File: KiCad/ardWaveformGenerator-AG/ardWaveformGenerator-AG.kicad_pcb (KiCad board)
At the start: 2 copper layers, 97.8 x 55.9 mm, 40 parts, among them SW1 SW_Rotary1x4, U1 Power in, U2 LM386, U3 Output

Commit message: ardWaveformGenerator-AG-pio with pcb-0.2
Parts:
- added R27: 10k, My_Misc:R_Axial_DIN0207_L6.3mm_D2.5mm_P10.16mm_Horizontal_large, F.Cu at (154.9, 107.6)
- added R28: 10k, My_Misc:R_Axial_DIN0207_L6.3mm_D2.5mm_P10.16mm_Horizontal_large, F.Cu at (154.9, 84.8)
- added R29: 10k, My_Misc:R_Axial_DIN0207_L6.3mm_D2.5mm_P10.16mm_Horizontal_large, F.Cu at (154.9, 72.1)
- added R30: 10k, My_Misc:R_Axial_DIN0207_L6.3mm_D2.5mm_P10.16mm_Horizontal_large, F.Cu at (150.5, 101.1)
- added R31: 10k, My_Misc:R_Axial_DIN0207_L6.3mm_D2.5mm_P10.16mm_Horizontal_large, F.Cu at (140.3, 97.9)
- added R32: 2.2k, My_Misc:R_Axial_DIN0207_L6.3mm_D2.5mm_P10.16mm_Horizontal_large, F.Cu at (150.5, 94.8)
- added R33: 220R, My_Misc:R_Axial_DIN0207_L6.3mm_D2.5mm_P10.16mm_Horizontal_large, F.Cu at (149.2, 81.0)
- added R34: 220R, My_Misc:R_Axial_DIN0207_L6.3mm_D2.5mm_P10.16mm_Horizontal_large, F.Cu at (146.1, 81.0)
- added R35: 220R, My_Misc:R_Axial_DIN0207_L6.3mm_D2.5mm_P10.16mm_Horizontal_large, F.Cu at (142.9, 81.0)
- added R36: 220R, My_Misc:R_Axial_DIN0207_L6.3mm_D2.5mm_P10.16mm_Horizontal_large, F.Cu at (139.7, 81.0)
- R1, R12, R14, R16, R18, R2, R20, R21, R4, R6: value 20k -> 10k; footprint My_Parts:R_Axial_parallell_DIN0207_L6.3mm_D2.5mm_P10.16mm_Horizontal_large -> My_Misc:R_Axial_DIN0207_L6.3mm_D2.5mm_P10.16mm_Horizontal_large
- R22: value 2.2k -> 10k
- R23, R24, R25, R26: value 220R -> 10k
- moved R26 113.0 mm to (158.1, 72.1)
- moved RV2 110.4 mm to (180.3, 125.4), turned to 180 degrees
- moved R25 103.8 mm to (158.1, 84.8)
- moved R11 102.9 mm to (186.7, 96.8), turned to 90 degrees
- moved R24 97.7 mm to (158.1, 107.6), turned to 90 degrees
- moved R23 95.0 mm to (161.3, 72.1)
- moved R10 91.6 mm to (170.8, 72.1), turned to -90 degrees
- moved R9 89.2 mm to (170.8, 84.8), turned to -90 degrees
- moved R8 87.0 mm to (170.8, 107.6), turned to 90 degrees
- moved R19 83.6 mm to (164.5, 84.8), turned to -90 degrees
- moved RV1 83.5 mm to (163.9, 124.4)
- moved R20 83.2 mm to (164.5, 72.1), turned to -90 degrees
- moved R2 82.8 mm to (183.5, 86.7), turned to -90 degrees
- moved D2 81.5 mm to (142.2, 77.2)
- moved D4 81.5 mm to (128.3, 77.2)
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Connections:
- A1 pad 27: D0 -> D12
- A1 pad 31: A4 -> unconnected-(A1-Pad31)
- A1 pad 32: A5 -> unconnected-(A1-Pad32)
- R1 pad 1: GND -> Net-(R1-Pad1)
- R1 pad 2: Net-(R1-Pad2) -> Net-(R5-Pad1)
- R10 pad 1: A2 -> D2
- R10 pad 2: +5V -> Net-(R10-Pad2)
- R11 pad 1: A3 -> A0
- R12 pad 1: D3 -> A1
- R12 pad 2: Net-(R12-Pad2) -> +5V
- R13 pad 1: Net-(R12-Pad2) -> A2
- R13 pad 2: Net-(R13-Pad2) -> +5V
- R14 pad 1: D4 -> A3
- R14 pad 2: Net-(R13-Pad2) -> +5V
- R15 pad 1: Net-(R13-Pad2) -> Net-(R8-Pad2)
- R15 pad 2: Net-(R15-Pad2) -> Net-(R18-Pad1)
- R16 pad 1: D5 -> Net-(R16-Pad1)
- R16 pad 2: Net-(R15-Pad2) -> Net-(R18-Pad1)
- R17 pad 1: Net-(R15-Pad2) -> D3
- R17 pad 2: Net-(R17-Pad2) -> Net-(R16-Pad1)
- R18 pad 1: D6 -> Net-(R18-Pad1)
- R18 pad 2: Net-(R17-Pad2) -> Net-(R18-Pad2)
- R19 pad 1: Net-(R17-Pad2) -> Net-(R19-Pad1)
- R19 pad 2: Net-(C1-Pad1) -> Net-(R18-Pad2)
- R2 pad 1: D0 -> GND
- R2 pad 2: Net-(R1-Pad2) -> Net-(R1-Pad1)
- R20 pad 1: D7 -> D4
- R20 pad 2: Net-(C1-Pad1) -> Net-(R19-Pad1)
- R21 pad 1: Net-(C1-Pad2) -> Net-(R18-Pad2)
- R22 pad 1: Net-(R21-Pad2) -> Net-(R22-Pad1)
- R22 pad 2: GND -> Net-(R21-Pad2)
- R23 pad 1: Net-(D1-Pad1) -> D5
- R23 pad 2: GND -> Net-(R22-Pad1)
- R24 pad 1: Net-(D2-Pad1) -> Net-(R21-Pad2)
- R24 pad 2: GND -> Net-(R24-Pad2)
- R25 pad 1: Net-(D3-Pad1) -> Net-(R25-Pad1)
- R25 pad 2: GND -> Net-(R24-Pad2)
- R26 pad 1: Net-(D4-Pad1) -> D6
- R26 pad 2: GND -> Net-(R25-Pad1)
- R3 pad 1: Net-(R1-Pad2) -> Net-(R3-Pad1)
- R3 pad 2: Net-(R3-Pad2) -> Net-(R5-Pad1)
- R4 pad 1: D1 -> D0
- R4 pad 2: Net-(R3-Pad2) -> Net-(R3-Pad1)
- R5 pad 1: Net-(R3-Pad2) -> Net-(R5-Pad1)
- R6 pad 1: D2 -> Net-(R6-Pad1)
- R7 pad 1: Net-(R5-Pad2) -> D1
- R7 pad 2: Net-(R12-Pad2) -> Net-(R6-Pad1)
- R8 pad 1: A0 -> Net-(R5-Pad2)
- R8 pad 2: +5V -> Net-(R8-Pad2)
- R9 pad 1: A1 -> Net-(R10-Pad2)
- R9 pad 2: +5V -> Net-(R8-Pad2)
- U2 pad 3: Net-(R21-Pad2) -> Net-(R31-Pad1)
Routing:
- net +5V: track 49.6 -> 126.4 mm, vias 0 -> 2
- net GND: track 234.4 -> 307.5 mm
- net A5: track 85.6 -> 17.9 mm
- net Net-(C1-Pad1): track 81.0 -> 19.3 mm
- net D0: track 64.3 -> 4.02 mm
- net A4: track 70.1 -> 12.0 mm
- net VCC: track 44.2 -> 91.4 mm
- net D2: track 42.3 -> 4.49 mm
- net D3: track 40.8 -> 4.79 mm
- net A0: track 19.1 -> 52.2 mm
- net D1: track 32.9 -> 4.23 mm
- net A1: track 23.3 -> 51.8 mm
- net D4: track 30.0 -> 5.09 mm
- net Net-(R5-Pad1): track 0.00 -> 23.1 mm
- net D8: track 28.6 -> 9.61 mm
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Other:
- board size 97.8 x 55.9 mm -> 80 x 66 mm
- board text added: "${TITLE}-${REVISION} Design: Jon SAgebrand github.com/jonsag"
- board text added: "1"
- board text removed: "${TITLE}-${REVISION} Design: Jon Sagebrand github.com/jonsag"
- board text removed: "Amplitude"
- board text removed: "Frequency"
- board text removed: "Power in"
- board text removed: "Pulse"
- board text removed: "Pulsewidth"
- board text removed: "Saw"
- board text removed: "Sine"
- board text removed: "Triangle"

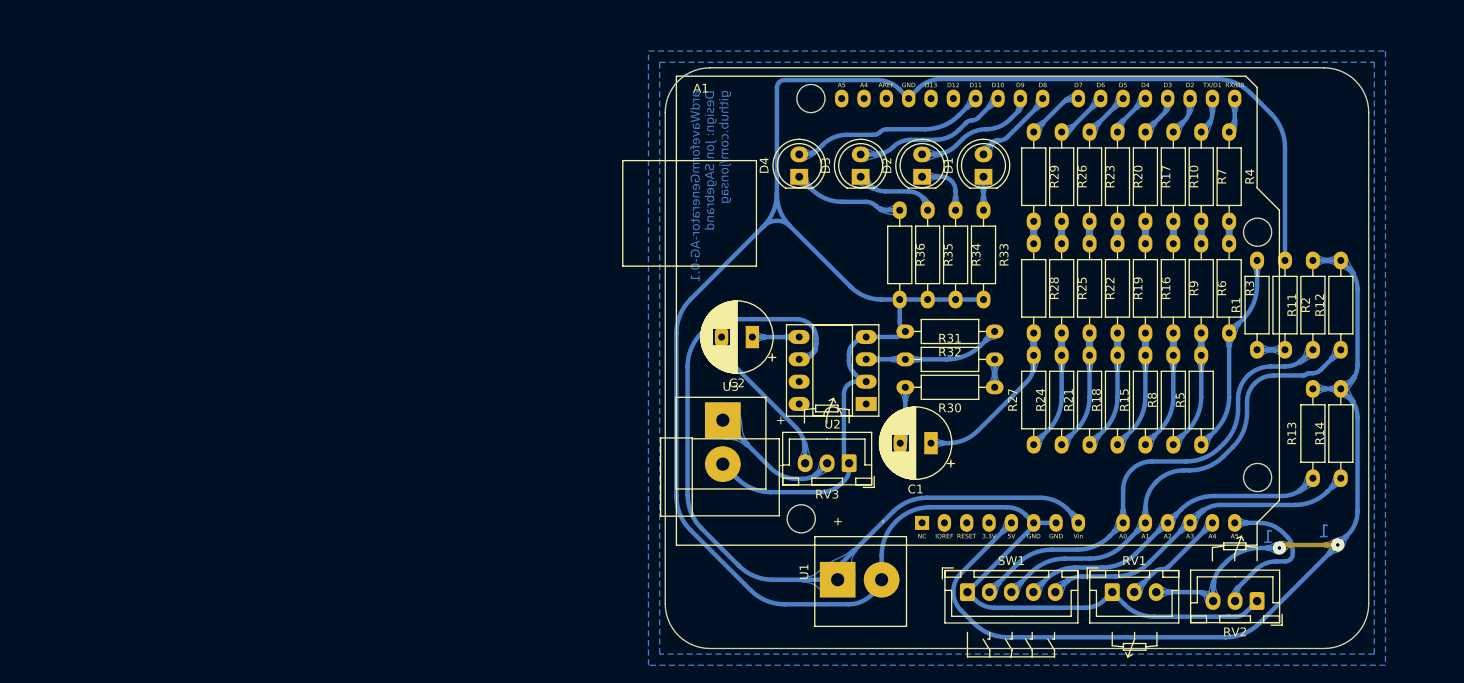
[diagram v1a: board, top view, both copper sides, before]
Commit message: LED-header on pcb, version 0.3
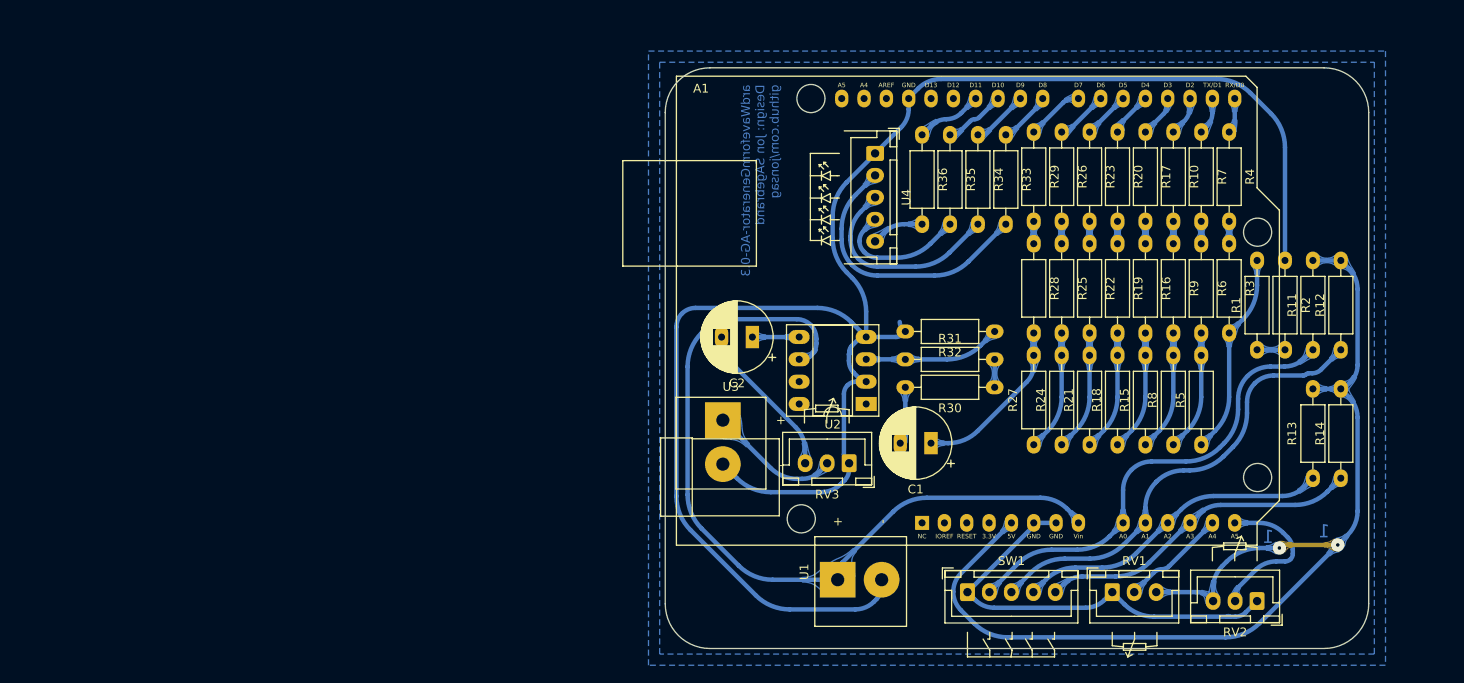
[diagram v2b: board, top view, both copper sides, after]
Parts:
- removed D1, D2, D3, D4: LED, My_Misc:LED_D5.0mm_large
- added U4: 5-pin_4_LED_header, My_Headers:5-pin JST 4-LED, F.Cu at (136.9, 74.5)
- moved R36 8.94 mm to (142.2, 72.4)
- moved R33 8.94 mm to (151.8, 72.4)
- moved R34 8.94 mm to (148.6, 72.4)
- moved R35 8.94 mm to (145.4, 72.4)
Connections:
- R33 pad 1: Net-(D1-Pad1) -> D8
- R33 pad 2: GND -> Net-(D1-Pad2)
- R34 pad 1: Net-(D2-Pad1) -> D9
- R34 pad 2: GND -> Net-(D2-Pad2)
- R35 pad 1: Net-(D3-Pad1) -> D10
- R35 pad 2: GND -> Net-(D3-Pad2)
- R36 pad 1: Net-(D4-Pad1) -> D11
- R36 pad 2: GND -> Net-(D4-Pad2)
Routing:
- net GND: track 307.5 -> 257.5 mm
- net Net-(D1-Pad2): track 0.00 -> 31.8 mm
- net Net-(D2-Pad2): track 0.00 -> 23.7 mm
- net Net-(D3-Pad2): track 0.00 -> 15.8 mm
- net D11: track 22.1 -> 7.58 mm
- net Net-(D4-Pad1): track 12.6 -> 0.00 mm
- net D10: track 17.7 -> 7.06 mm
- net Net-(D3-Pad1): track 9.42 -> 0.00 mm
- net D9: track 13.9 -> 6.52 mm
- net Net-(D2-Pad1): track 6.90 -> 0.00 mm
- net Net-(D4-Pad2): track 0.00 -> 5.99 mm
- net Net-(D1-Pad1): track 3.81 -> 0.00 mm
- net D8: track 9.61 -> 6.07 mm

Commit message: new buttons
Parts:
- removed SW1: SW_Rotary1x4, My_Headers:5-pin JST SW_Rotary1x4
- added U2: 5-pin_4_buttons_+_common, My_Headers:5-pin JST 4 buttons + common, F.Cu at (147.3, 124.5)
- renumbered U2 to U3, U3 to U4, U4 to U5

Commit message: VeroRoute and AG v0.4
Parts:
- R1, R10, R11, R12, R13, R14, R15, R16, R17, R18, R19, R2, R20, R21, R22, R23, R24, R25, R26, R27, R28, R29, R3, R30, R31, R32, R33, R34, R35, R36, R4, R5, R6, R7, R8, R9: footprint My_Misc:R_Axial_DIN0207_L6.3mm_D2.5mm_P10.16mm_Horizontal_large -> My_Misc:R_Axial_DIN0207_L6.3mm_D2.5mm_P2.54mm_Vertical_large
- moved U5 34.6 mm to (165.1, 94.6), turned to 180 degrees
- moved R11 24.7 mm to (163.2, 104.5)
- moved R12 24.7 mm to (166.4, 104.5)
- moved U2 21.2 mm to (162.7, 109.9)
- moved R15 20.9 mm to (183.5, 94.0)
- moved R18 20.9 mm to (180.3, 94.0)
- moved R21 20.9 mm to (177.2, 94.0)
- moved R24 20.9 mm to (174.0, 94.0)
- moved R27 20.9 mm to (170.8, 94.0)
- moved R5 20.9 mm to (189.9, 94.0)
- moved R8 20.9 mm to (186.7, 94.0)
- moved RV1 20.9 mm to (179.1, 110.1)
- moved R13 18.5 mm to (169.5, 104.5)
- moved R14 18.5 mm to (172.7, 104.5)
- moved RV2 18.4 mm to (190.5, 110.1), turned to 0 degrees
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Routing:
- net +5V: track 126.4 -> 94.3 mm
- net A1: track 51.8 -> 27.1 mm
- net A0: track 52.2 -> 28.1 mm
- net Net-(D1-Pad2): track 31.8 -> 12.6 mm
- net GND: track 257.5 -> 238.6 mm, vias 0 -> 2
- net Net-(R1-Pad2): track 23.1 -> 6.36 mm
- net Net-(C1-Pad1): track 19.3 -> 35.2 mm
- net Net-(D2-Pad2): track 23.7 -> 12.3 mm
- net A3: track 37.0 -> 26.9 mm
- net A2: track 36.2 -> 26.9 mm
- net Net-(R21-Pad2): track 13.8 -> 6.36 mm
- net Net-(R15-Pad1): track 13.8 -> 6.36 mm
- net Net-(R24-Pad2): track 13.8 -> 6.36 mm
- net Net-(R5-Pad2): track 13.8 -> 6.36 mm
- net Net-(R18-Pad2): track 13.8 -> 6.36 mm
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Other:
- board size 80 x 66 mm -> 70.5 x 55.9 mm
- board text added: "${TITLE}-${REVISION} github.com/jonsag"
- board text added: "2"
- board text added: "3"
- board text removed: "${TITLE}-${REVISION} Design: Jon SAgebrand github.com/jonsag"

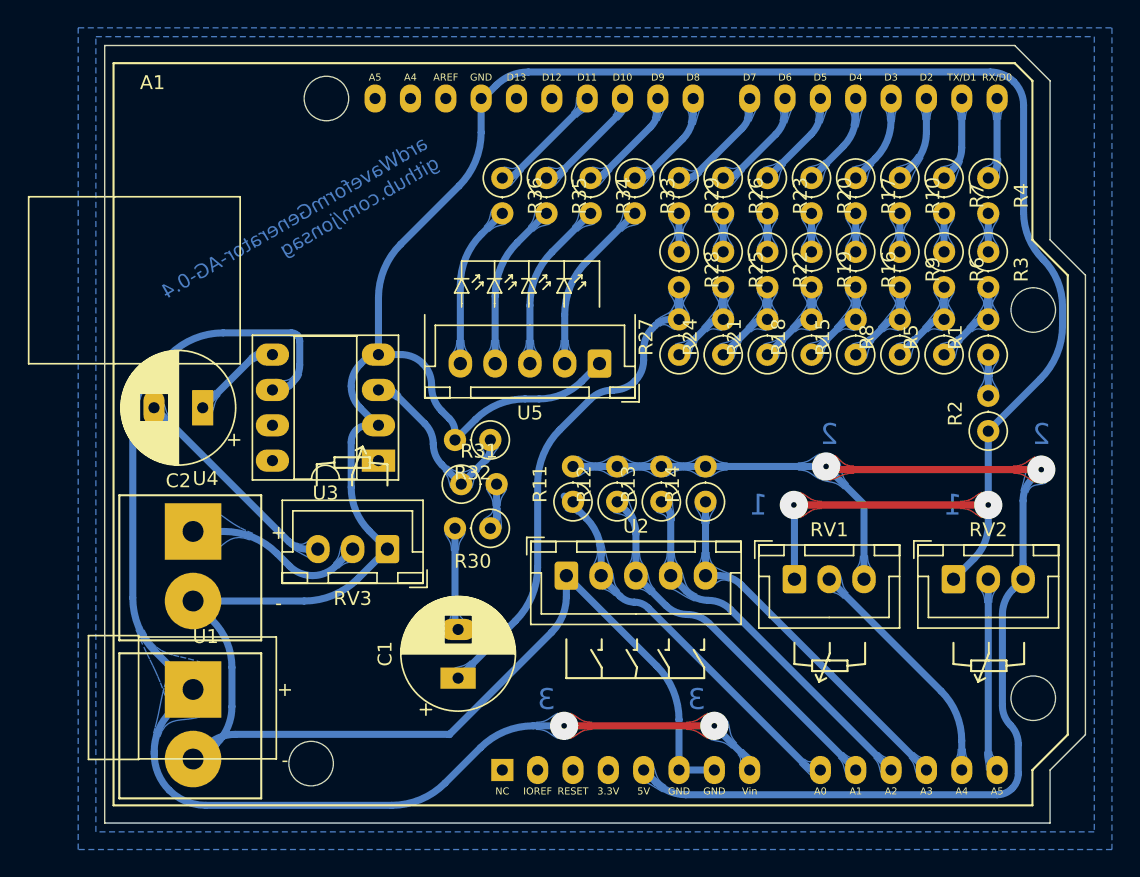
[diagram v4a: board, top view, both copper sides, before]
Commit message: wider tracks v0.5
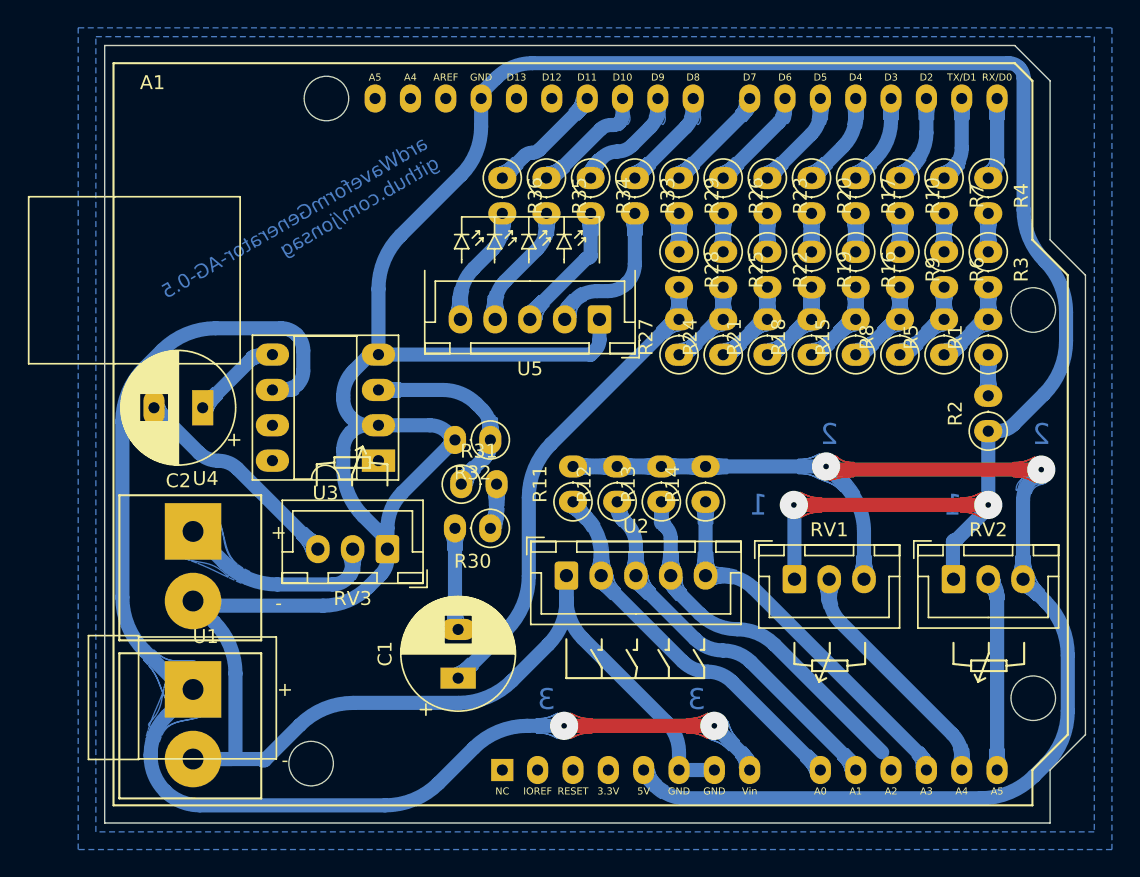
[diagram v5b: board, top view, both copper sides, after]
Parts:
- moved U5 3.17 mm to (165.1, 91.4)
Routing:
- net GND: track 238.6 -> 262.2 mm
- net Net-(D4-Pad2): track 11.8 -> 8.60 mm
- net Net-(D3-Pad2): track 12.1 -> 8.92 mm
- net Net-(D2-Pad2): track 12.3 -> 9.48 mm
- net +5V: track 94.3 -> 96.8 mm
- net VCC: track 95.2 -> 97.4 mm
- net Net-(D1-Pad2): track 12.6 -> 10.9 mm
- net Net-(RV3-Pad2): track 13.1 -> 14.7 mm
- net A2: track 26.9 -> 25.9 mm
- net Net-(C1-Pad1): track 35.2 -> 34.2 mm
- net Net-(R31-Pad1): track 13.5 -> 14.2 mm
- net A0: track 28.1 -> 27.4 mm
